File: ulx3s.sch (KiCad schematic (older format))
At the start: 9 parts, among them IC1 MT48LC16M4A2P, U1 LFE5U-25F-6BG381C, U2 ESP-12E

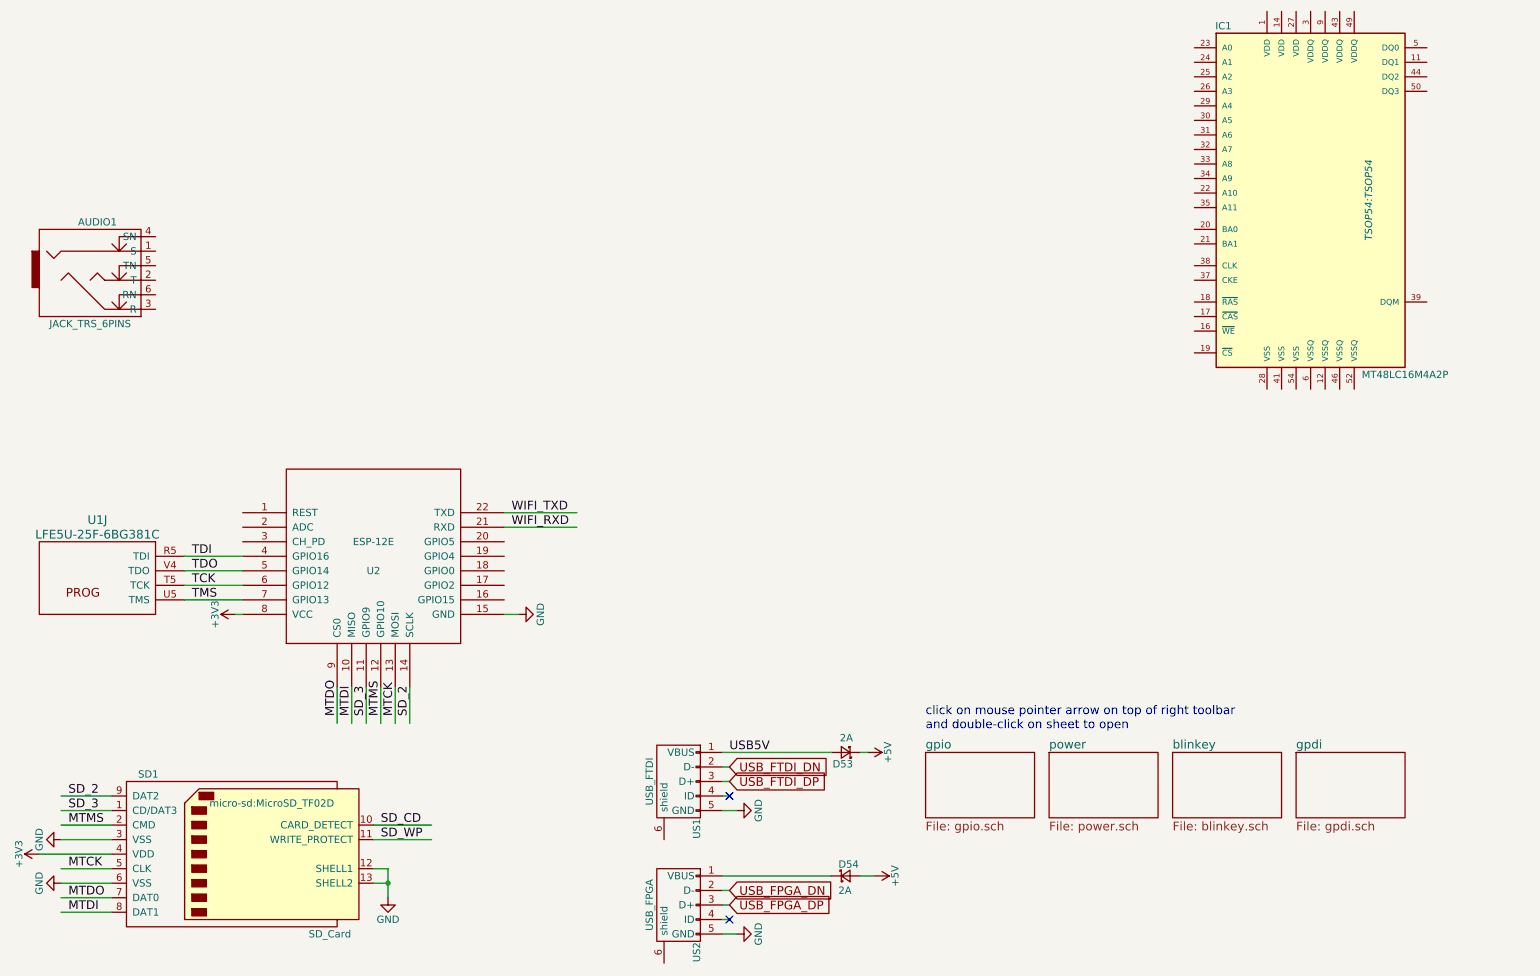
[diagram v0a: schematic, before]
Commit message: move usb to "usbserial" sheet and add ft2232 footprint move sdram to "ram" sheet create "wifi" sheet
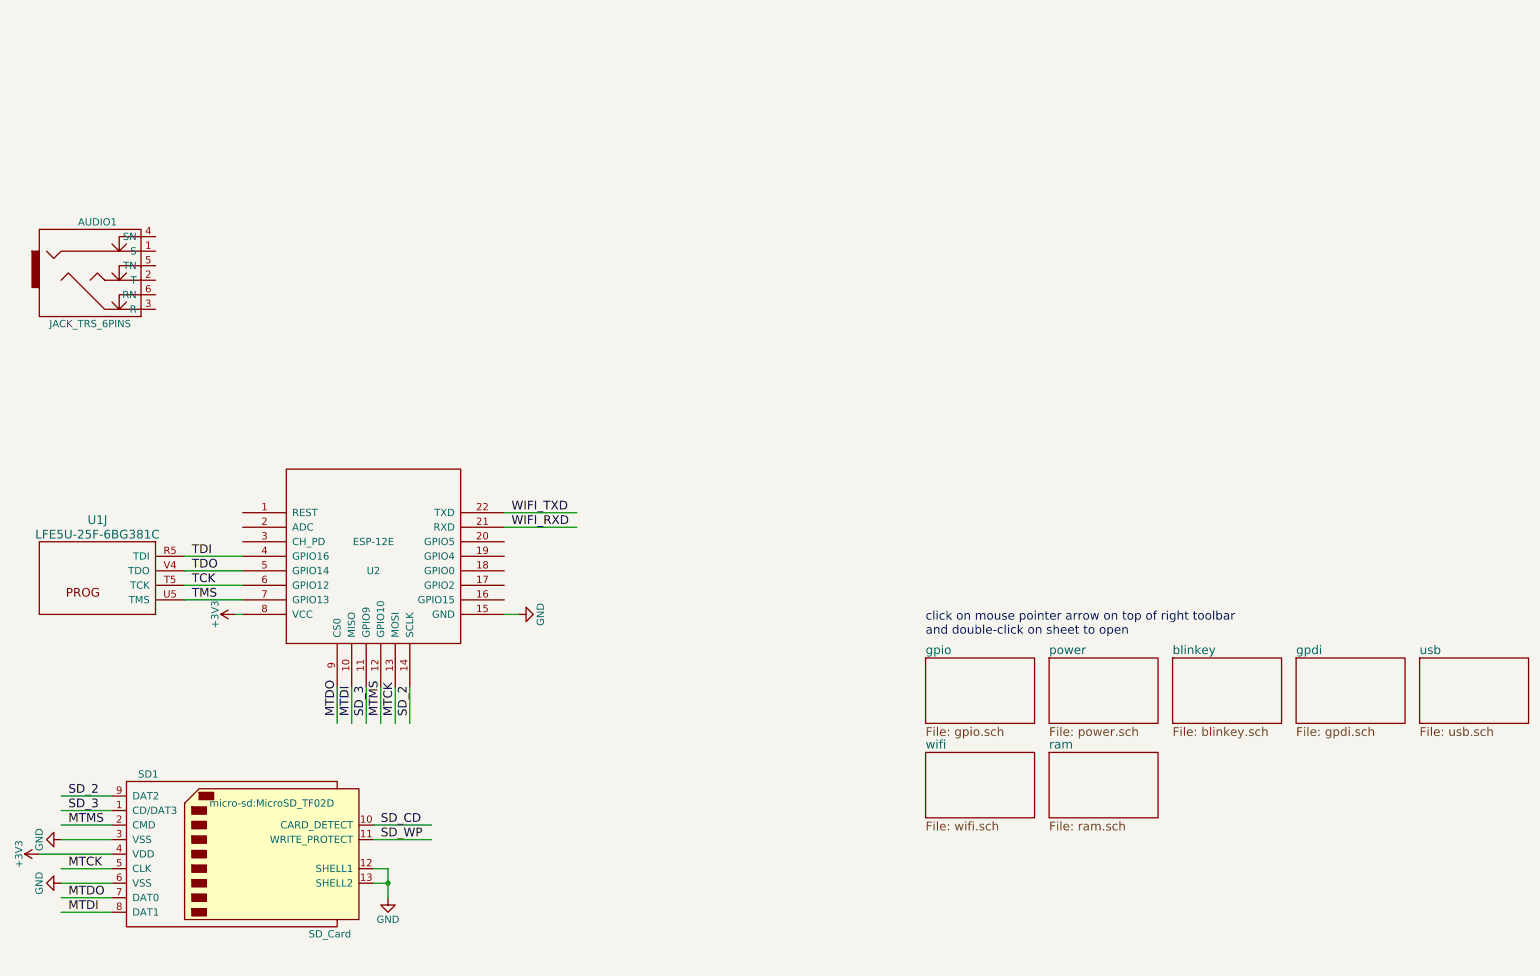
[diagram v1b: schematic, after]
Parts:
- removed D53, D54: 2A, SMD_Packages:SMD-1206_Pol, symbol D_Schottky_Small
- removed IC1: MT48LC16M4A2P, TSOP54:TSOP54, symbol MT48LC16M4A2P
- removed US1: USB_FTDI, usb_otg:USB_Micro-B, symbol USB_OTG
- removed US2: USB_FPGA, usb_otg:USB_Micro-B, symbol USB_OTG
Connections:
- net labels removed: +5V, USB5V, USB_FPGA_DN, USB_FPGA_DP, USB_FTDI_DN, USB_FTDI_DP
- wire segments 40 -> 28
- no-connect marks 2 -> 0
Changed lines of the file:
@@
 LIBS:micro-hdmi-d
 LIBS:ap3429a
+LIBS:ft2232
 LIBS:ulx3s-cache
 EELAYER 25 0
@@
 $Descr A4 11693 8268
 encoding utf-8
-Sheet 1 5
+Sheet 1 8
 Title "ULX3S"
 Date ""
@@
 	1    1300 2650
 	1    0    0    -1
-$EndComp
-$Comp
-L D_Schottky_Small D53
-U 1 1 56AA1324
-P 6450 5900
-F 0 "D53" H 6400 5980 50  0000 L CNN
-F 1 "2A" H 6400 5800 50  0000 L CNN
-F 2 "SMD_Packages:SMD-1206_Pol" V 6450 5900 60  0001 C CNN
-F 3 "" V 6450 5900 60  0000 C CNN
-	1    6450 5900
-	-1   0    0    1
-$EndComp
-Wire Wire Line
-	5600 5900 6350 5900
-Wire Wire Line
-	6550 5900 6600 5900
-$Comp
-L +5V #PWR02
-U 1 1 56AA16D2
-P 6600 5900
-F 0 "#PWR02" H 6600 5750 50  0001 C CNN
-F 1 "+5V" H 6600 6040 50  0000 C CNN
-F 2 "" H 6600 5900 60  0000 C CNN
-F 3 "" H 6600 5900 60  0000 C CNN
-	1    6600 5900
-	0    1    1    0
-$EndComp
-Text Label 5650 5900 0    60   ~ 0
-USB5V
-Wire Wire Line
-	6550 6750 6650 6750
-$Comp
-L D_Schottky_Small D54
-U 1 1 56AA2821
-P 6450 6750
-F 0 "D54" H 6400 6830 50  0000 L CNN
-F 1 "2A" H 6400 6650 50  0000 L CNN
-F 2 "SMD_Packages:SMD-1206_Pol" V 6450 6750 60  0001 C CNN
-F 3 "" V 6450 6750 60  0000 C CNN
-	1    6450 6750
-	1    0    0    -1
-$EndComp
-Wire Wire Line
-	5600 6750 6350 6750
-$Comp
-L +5V #PWR03
-U 1 1 56AA305B
-P 6650 6750
-F 0 "#PWR03" H 6650 6600 50  0001 C CNN
-F 1 "+5V" H 6650 6890 50  0000 C CNN
-F 2 "" H 6650 6750 60  0000 C CNN
-F 3 "" H 6650 6750 60  0000 C CNN
-	1    6650 6750
-	0    1    1    0
 $EndComp
 $Comp
@@
 MTDI
 $Sheet
-S 7000 5900 750  450
+S 7000 5250 750  450
 U 56AC389C
 F0 "gpio" 60
 F1 "gpio.sch" 60
 $EndSheet
-$Comp
-L USB_OTG US1
-U 1 1 58D432CE
-P 5300 6100
-F 0 "US1" H 5625 5975 50  0000 C CNN
-F 1 "USB_FTDI" H 5300 6300 50  0000 C CNN
-F 2 "usb_otg:USB_Micro-B" V 5250 6000 50  0001 C CNN
-F 3 "" V 5250 6000 50  0000 C CNN
-	1    5300 6100
-	0    -1   1    0
-$EndComp
-$Comp
-L USB_OTG US2
-U 1 1 58D4378B
-P 5300 6950
-F 0 "US2" H 5625 6825 50  0000 C CNN
-F 1 "USB_FPGA" H 5300 7150 50  0000 C CNN
-F 2 "usb_otg:USB_Micro-B" V 5250 6850 50  0001 C CNN
-F 3 "" V 5250 6850 50  0000 C CNN
-	1    5300 6950
-	0    -1   1    0
-$EndComp
-$Comp
-L GND #PWR04
-U 1 1 58D43846
-P 5700 6300
-F 0 "#PWR04" H 5700 6050 50  0001 C CNN
-F 1 "GND" H 5700 6150 50  0000 C CNN
-F 2 "" H 5700 6300 50  0000 C CNN
-F 3 "" H 5700 6300 50  0000 C CNN
-	1    5700 6300
-	0    -1   -1   0
-$EndComp
-Wire Wire Line
-	5600 6300 5700 6300
-Wire Wire Line
-	5600 7150 5700 7150
-$Comp
-L GND #PWR05
-U 1 1 58D43AF2
-P 5700 7150
-F 0 "#PWR05" H 5700 6900 50  0001 C CNN
-F 1 "GND" H 5700 7000 50  0000 C CNN
-F 2 "" H 5700 7150 50  0000 C CNN
-F 3 "" H 5700 7150 50  0000 C CNN
-	1    5700 7150
-	0    -1   -1   0
-$EndComp
-$Sheet
-S 7850 5900 750  450
+$Sheet
+S 7850 5250 750  450
 U 58D51CAD
 F0 "power" 60
@@
 	1050 6800 1400 6800
 $Comp
-L GND #PWR06
+L GND #PWR02
 U 1 1 58D58197
 P 1050 6500
-F 0 "#PWR06" H 1050 6250 50  0001 C CNN
+F 0 "#PWR02" H 1050 6250 50  0001 C CNN
 F 1 "GND" H 1050 6350 50  0000 C CNN
 F 2 "" H 1050 6500 50  0000 C CNN
@@
 $EndComp
 $Comp
-L GND #PWR07
+L GND #PWR03
 U 1 1 58D581BF
 P 1050 6800
-F 0 "#PWR07" H 1050 6550 50  0001 C CNN
+F 0 "#PWR03" H 1050 6550 50  0001 C CNN
 F 1 "GND" H 1050 6650 50  0000 C CNN
 F 2 "" H 1050 6800 50  0000 C CNN
@@
 SD_WP
 $Comp
-L GND #PWR08
+L GND #PWR04
 U 1 1 58D58733
 P 3300 6900
-F 0 "#PWR08" H 3300 6650 50  0001 C CNN
+F 0 "#PWR04" H 3300 6650 50  0001 C CNN
 F 1 "GND" H 3300 6750 50  0000 C CNN
 F 2 "" H 3300 6900 50  0000 C CNN
@@
 Connection ~ 3300 6800
 $Comp
-L +3V3 #PWR09
+L +3V3 #PWR05
 U 1 1 58D5F08C
 P 2250 4950
-F 0 "#PWR09" H 2250 4800 50  0001 C CNN
+F 0 "#PWR05" H 2250 4800 50  0001 C CNN
 F 1 "+3V3" H 2250 5090 50  0000 C CNN
 F 2 "" H 2250 4950 50  0000 C CNN
@@
 $EndComp
 $Comp
-L +3V3 #PWR010
+L +3V3 #PWR06
 U 1 1 58D5F123
 P 900 6600
-F 0 "#PWR010" H 900 6450 50  0001 C CNN
+F 0 "#PWR06" H 900 6450 50  0001 C CNN
 F 1 "+3V3" H 900 6740 50  0000 C CNN
 F 2 "" H 900 6600 50  0000 C CNN
@@
 	0    -1   -1   0
 $EndComp
-Text GLabel 5650 6000 2    60   Input ~ 0
-USB_FTDI_DN
-Text GLabel 5650 6100 2    60   Input ~ 0
-USB_FTDI_DP
-Wire Wire Line
-	5600 6000 5650 6000
-Wire Wire Line
-	5600 6100 5650 6100
-Text GLabel 5650 6850 2    60   Input ~ 0
-USB_FPGA_DN
-Text GLabel 5650 6950 2    60   Input ~ 0
-USB_FPGA_DP
-Wire Wire Line
-	5600 6850 5650 6850
-Wire Wire Line
-	5600 6950 5650 6950
-Wire Wire Line
-	5600 7050 5650 7050
-NoConn ~ 5650 7050
-Wire Wire Line
-	5600 6200 5650 6200
-NoConn ~ 5650 6200
-$Comp
-L MT48LC16M4A2P IC1
-U 1 1 58D5C787
-P 9650 2100
-F 0 "IC1" H 9050 3300 50  0000 C CNN
-F 1 "MT48LC16M4A2P" H 10300 900 50  0000 C CNN
-F 2 "TSOP54:TSOP54" V 10050 2100 50  0000 C CIN
-F 3 "" H 9650 1850 50  0000 C CNN
-	1    9650 2100
-	1    0    0    -1
-$EndComp
-$Sheet
-S 8700 5900 750  450
+$Sheet
+S 8700 5250 750  450
 U 58D6547C
 F0 "blinkey" 60
 F1 "blinkey.sch" 60
 $EndSheet
-Text Notes 7000 5750 0    60   ~ 0
+Text Notes 7000 5100 0    60   ~ 0
 click on mouse pointer arrow on top of right toolbar\nand double-click on sheet to open
 $Sheet
-S 9550 5900 750  450
+S 9550 5250 750  450
 U 58D686D9
 F0 "gpdi" 60
 F1 "gpdi.sch" 60
 $EndSheet
+$Sheet
+S 10400 5250 750  450
+U 58D6BF46
+F0 "usb" 60
+F1 "usb.sch" 60
+$EndSheet
+$Sheet
+S 7000 5900 750  450
+U 58D6D447
+F0 "wifi" 60
+F1 "wifi.sch" 60
+$EndSheet
+$Sheet
+S 7850 5900 750  450
+U 58D6D507
+F0 "ram" 60
+F1 "ram.sch" 60
+$EndSheet
 $EndSCHEMATC
